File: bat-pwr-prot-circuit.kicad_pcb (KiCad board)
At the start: 2 copper layers, 51.8 x 19.5 mm, 14 parts, among them IC1 FS312F-G, IC2 3v3 V-Reg, J1 Bat+, J2 3v3, J3 Battery, J4 Bat+, J5 3v3, J6 Chg, Q1 FS8205

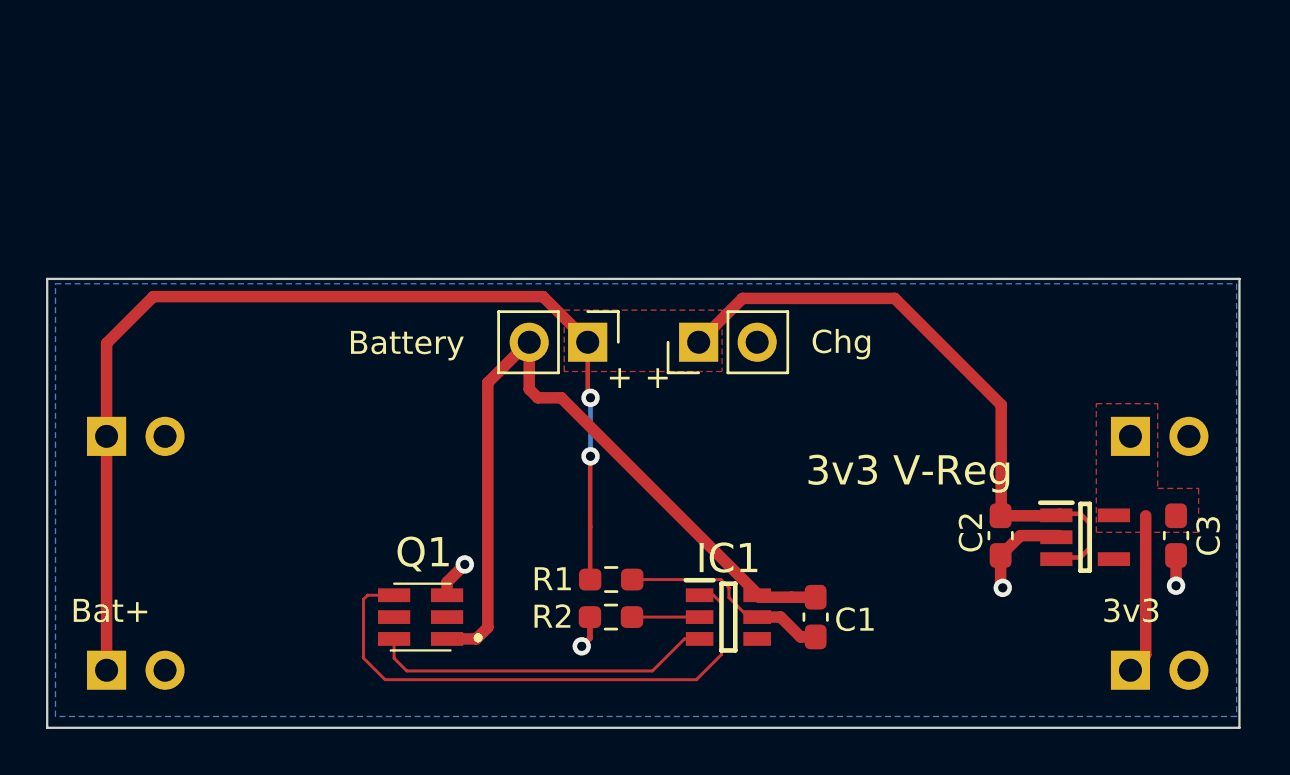
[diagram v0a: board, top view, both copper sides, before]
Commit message: Selectable rails and led indicators
- Added pin selectory to configure the left and right rail connectors individually for batt+ and 3v3
- Added led indicators for batt+ and 3v3
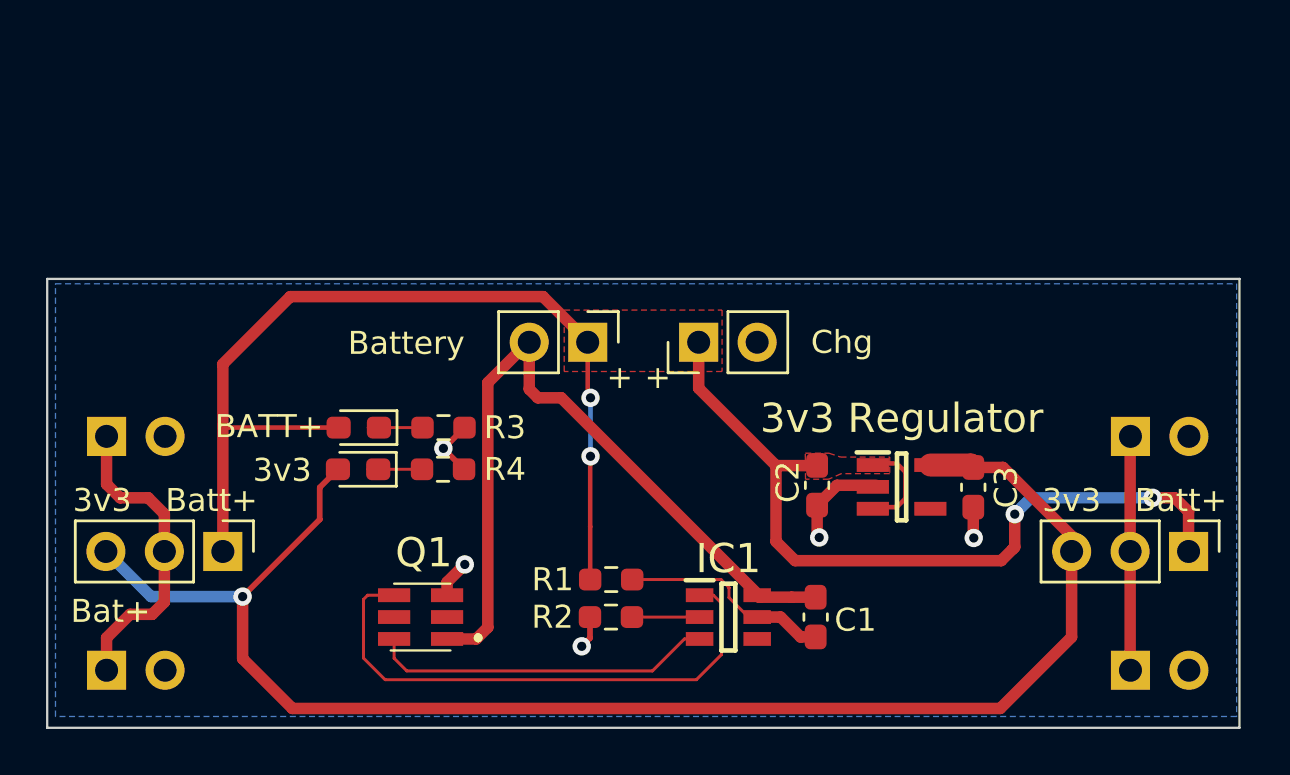
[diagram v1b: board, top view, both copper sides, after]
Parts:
- added D1: BATT+, LED_SMD:LED_0603_1608Metric_Pad1.05x0.95mm_HandSolder, F.Cu at (150.3, 89.6)
- added D2: 3v3, LED_SMD:LED_0603_1608Metric_Pad1.05x0.95mm_HandSolder, F.Cu at (150.3, 91.4)
- added JL1: Conn_01x03, Connector_PinHeader_2.54mm:PinHeader_1x03_P2.54mm_Vertical, F.Cu at (144.4, 94.9)
- added JR1: Conn_01x03, Connector_PinHeader_2.54mm:PinHeader_1x03_P2.54mm_Vertical, F.Cu at (186.4, 94.9)
- added R3: 680, Resistor_SMD:R_0603_1608Metric_Pad0.98x0.95mm_HandSolder, F.Cu at (154.0, 89.6)
- added R4: 680, Resistor_SMD:R_0603_1608Metric_Pad0.98x0.95mm_HandSolder, F.Cu at (154.0, 91.4)
- IC2: value 3v3 V-Reg -> 3v3 Regulator
- moved C3 9.06 mm to (177.0, 92.2)
- moved C2 8.27 mm to (170.2, 92.1)
- moved IC2 8.27 mm to (173.9, 92.1)
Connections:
- J1 pad 1: /BATT+ -> /Left
- J2 pad 1: +3V3 -> /Right
- J4 pad 1: /BATT+ -> /Left
- J5 pad 1: +3V3 -> /Right
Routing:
- net +3V3: track 6.99 -> 66.7 mm, vias 0 -> 1
- net /Left: track 0.00 -> 13.5 mm
- net /Right: track 0.00 -> 10.2 mm
- net /BATT+: track 74.4 -> 79.5 mm, vias 2 -> 4
- net GND: track 8.75 -> 11.4 mm, vias 4 -> 5
- net Net-(D2-Pad1): track 0.00 -> 2.37 mm
- net Net-(D1-Pad1): track 0.00 -> 2.36 mm
- removed copper zone on F.Cu, net +3V3
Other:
- board text added: "3v3"
- board text added: "Batt+"

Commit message: Revision 1.1 commit
- Separated power lines to Bat+ and 3v3
- Added selector pins for each side of the board
- Added mounting holes
- Improved the labeling on the front
- Added logo
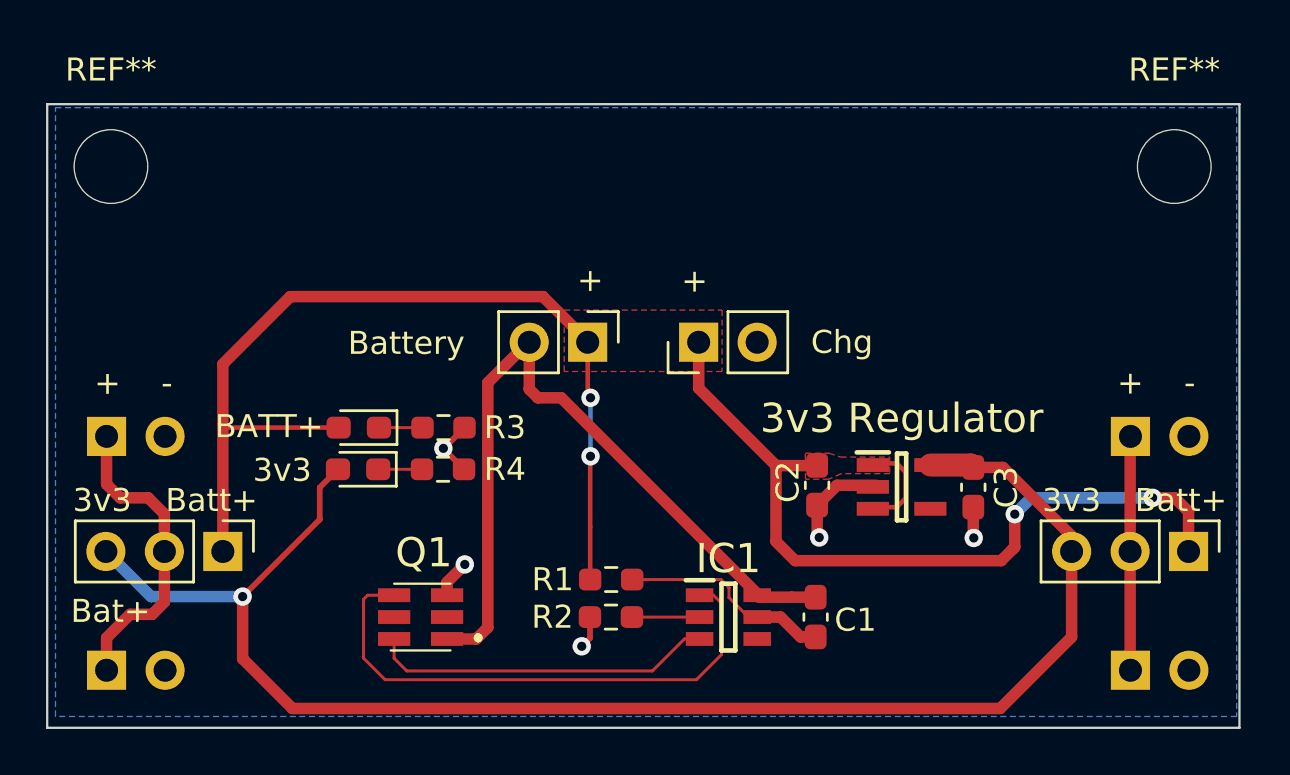
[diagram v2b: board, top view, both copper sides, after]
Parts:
- added G***: LOGO, LOGO, B.Cu at (175.9, 85.4)
- added REF**: MountingHole_3.2mm_M3, MountingHole:MountingHole_3.2mm_M3, F.Cu at (185.8, 78.2)
- added REF**: MountingHole_3.2mm_M3, MountingHole:MountingHole_3.2mm_M3, F.Cu at (139.6, 78.2)
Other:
- board size 51.8 x 19.5 mm -> 51.8 x 27.1 mm
- board text added: "-"
- board text added: "Battery Protection 3v3 v1.1 (2023)"
- board text removed: "Battery Protection 3v3 (Rev 1.0) (c) 2022 chof.org"

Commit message: Updated template for KiCAD 7
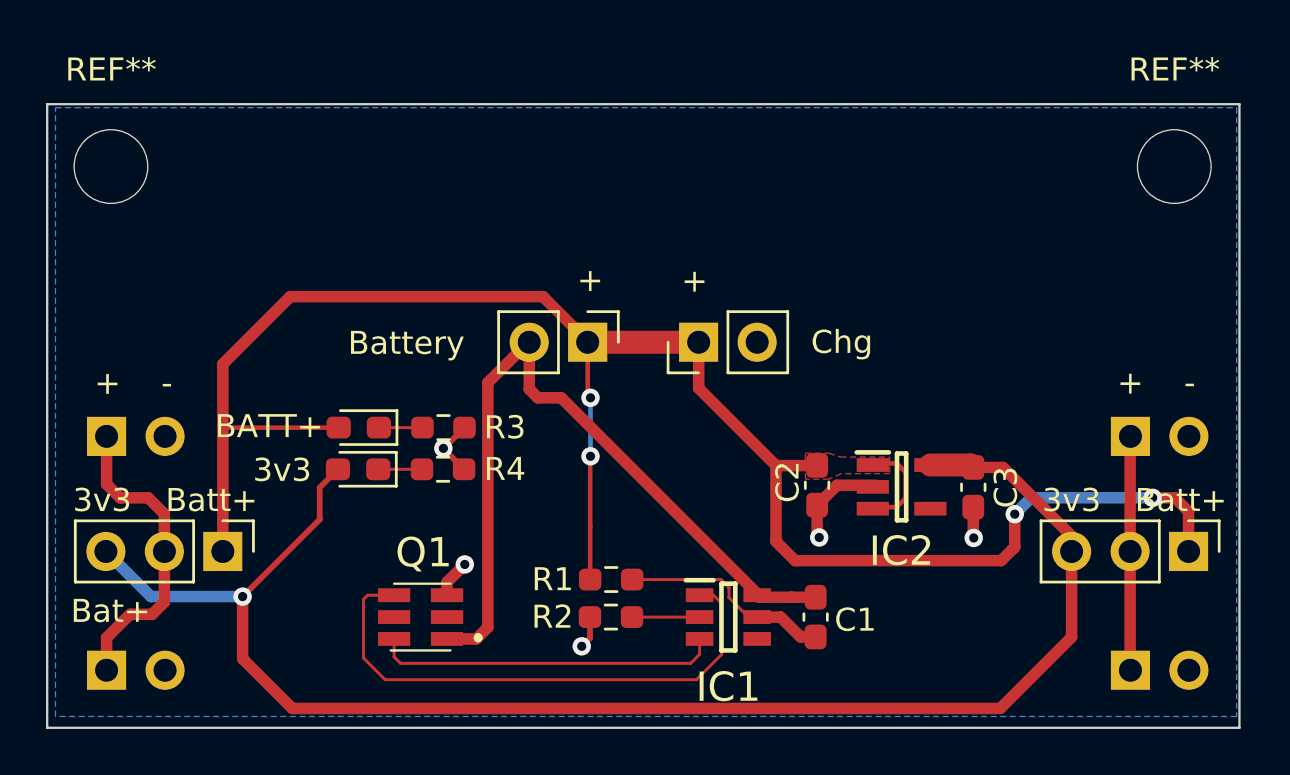
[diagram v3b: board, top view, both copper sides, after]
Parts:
- G***: footprint LOGO -> Chof747 Logos:LOGO large
- IC1: footprint footprints:SOT95P280X145-6N -> Chof747 Footprints:SOT95P280X145-6N
- IC2: footprint footprints:SOT95P270X145-5N -> Chof747 Footprints:SOT95P270X145-5N
- Q1: footprint footprints:FS8205 -> Chof747 Footprints:FS8205
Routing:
- net /BATT+: track 79.5 -> 84.4 mm
